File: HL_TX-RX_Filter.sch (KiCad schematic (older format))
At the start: 184 parts, among them J1 To Antenna, J2 From Tx, J3 ICSP, J4 Data In, J5 SCL SDA, J6 To Rx in, Q1 2N7002, Q2 2N7002, Q3 2N7002, Q4 2N7002, Q5 2N7002, Q6 2N7002, Q7 2N7002, Q8 2N7002, U1 LD1117S33TR, U10 PE4259, U11 PE4259, U12 PE4259, U13 PE4259, U2 ATMEGA328-AU, U3 PE4259, U4 PE4259, U5 PE4259, U6 PE4259, U7 PE4259, U8 PE4259, U9 PE4259

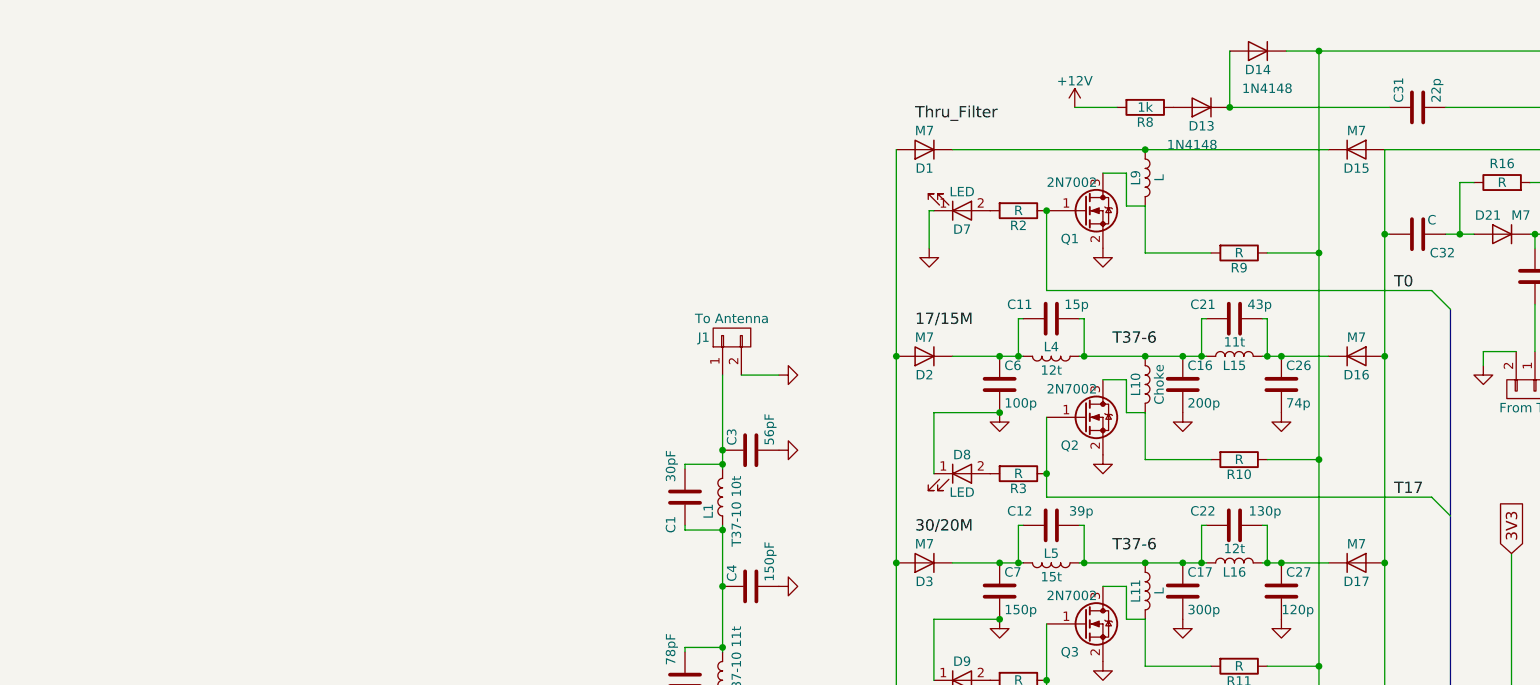
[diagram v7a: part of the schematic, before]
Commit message: More progress with Tx filter board layout
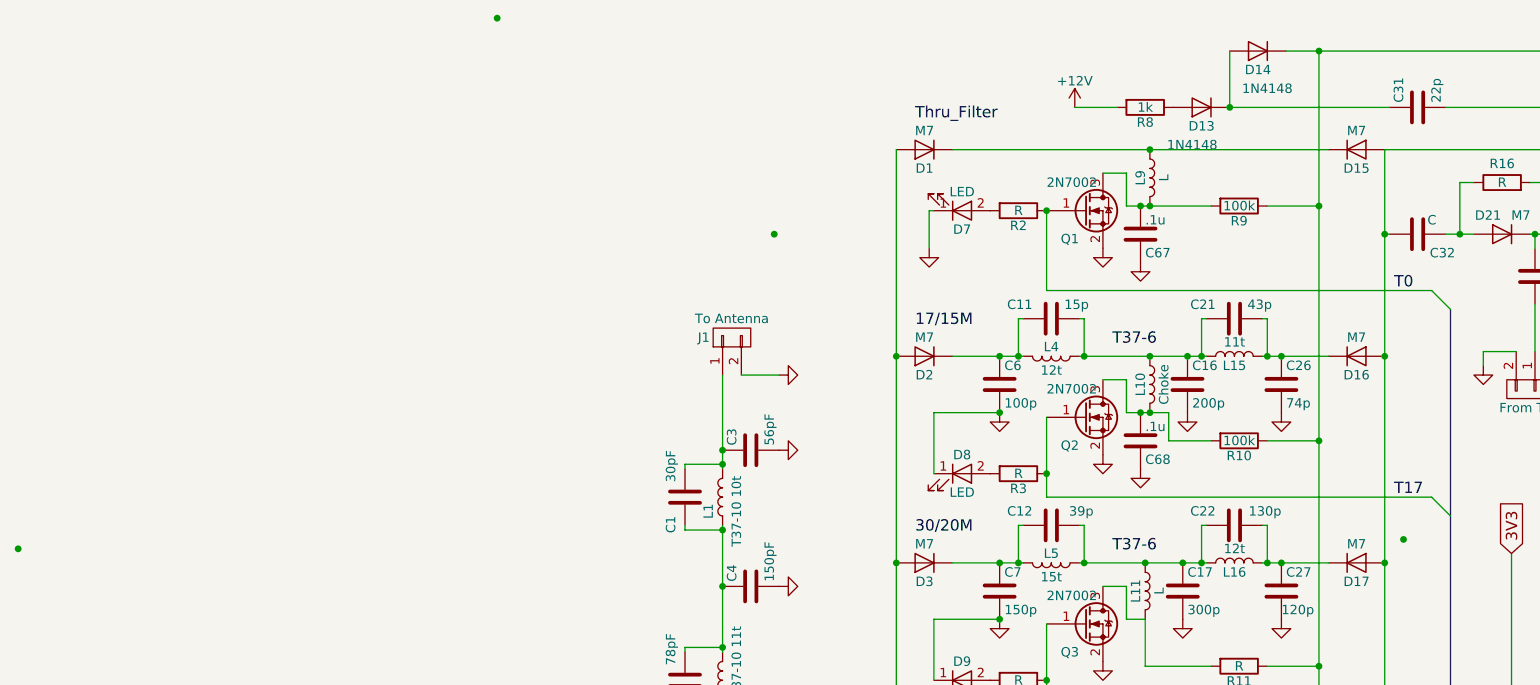
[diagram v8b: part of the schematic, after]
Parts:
- added C67, C68: .1u, Capacitors_SMD:C_1206_HandSoldering, symbol C
- R10, R9: value R -> 100k
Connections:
- net GND: now also C67.2, C68.2
- net at L10.2, Q2.3 (D), R10.2: now also C68.1
- net at L9.2, Q1.3 (D), R9.2: now also C67.1
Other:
- moved on the sheet: C16, L10, L9, R10, R9
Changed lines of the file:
@@
 L C C16
 U 1 1 58EF6AB2
-P 3475 2375
-F 0 "C16" H 3500 2475 50  0000 L CNN
-F 1 "200p" H 3500 2275 50  0000 L CNN
-F 2 "Capacitors_SMD:C_1206_HandSoldering" H 3513 2225 50  0001 C CNN
-F 3 "" H 3475 2375 50  0001 C CNN
-	1    3475 2375
+P 3500 2375
+F 0 "C16" H 3525 2475 50  0000 L CNN
+F 1 "200p" H 3525 2275 50  0000 L CNN
+F 2 "Capacitors_SMD:C_1206_HandSoldering" H 3538 2225 50  0001 C CNN
+F 3 "" H 3500 2375 50  0001 C CNN
+	1    3500 2375
 	1    0    0    -1
 $EndComp
@@
 L GND #PWR027
 U 1 1 58EF6AB8
-P 3475 2525
-F 0 "#PWR027" H 3475 2275 50  0001 C CNN
-F 1 "GND" H 3475 2375 50  0001 C CNN
-F 2 "" H 3475 2525 50  0001 C CNN
-F 3 "" H 3475 2525 50  0001 C CNN
-	1    3475 2525
+P 3500 2525
+F 0 "#PWR027" H 3500 2275 50  0001 C CNN
+F 1 "GND" H 3500 2375 50  0001 C CNN
+F 2 "" H 3500 2525 50  0001 C CNN
+F 3 "" H 3500 2525 50  0001 C CNN
+	1    3500 2525
 	1    0    0    -1
 $EndComp
@@
 L L L10
 U 1 1 58EF6AE3
-P 3275 2375
-F 0 "L10" V 3225 2375 50  0000 C CNN
-F 1 "Choke" V 3350 2375 50  0000 C CNN
-F 2 "Inductors_G:BalunCoreChoke" H 3275 2375 50  0001 C CNN
-F 3 "" H 3275 2375 50  0001 C CNN
-	1    3275 2375
+P 3300 2375
+F 0 "L10" V 3250 2375 50  0000 C CNN
+F 1 "Choke" V 3375 2375 50  0000 C CNN
+F 2 "Inductors_G:BalunCoreChoke" H 3300 2375 50  0001 C CNN
+F 3 "" H 3300 2375 50  0001 C CNN
+	1    3300 2375
 	1    0    0    -1
 $EndComp
@@
 L R R10
 U 1 1 58EF6AFC
-P 3775 2775
-F 0 "R10" V 3855 2775 50  0000 C CNN
-F 1 "R" V 3775 2775 50  0000 C CNN
-F 2 "Resistors_SMD:R_1206_HandSoldering" V 3705 2775 50  0001 C CNN
-F 3 "" H 3775 2775 50  0001 C CNN
-	1    3775 2775
+P 3775 2675
+F 0 "R10" V 3855 2675 50  0000 C CNN
+F 1 "100k" V 3775 2675 50  0000 C CNN
+F 2 "Resistors_SMD:R_1206_HandSoldering" V 3705 2675 50  0001 C CNN
+F 3 "" H 3775 2675 50  0001 C CNN
+	1    3775 2675
 	0    1    1    0
 $EndComp
@@
 L L L9
 U 1 1 58F03CDB
-P 3275 1275
-F 0 "L9" V 3225 1275 50  0000 C CNN
-F 1 "L" V 3350 1275 50  0000 C CNN
-F 2 "Inductors_G:BalunCoreChoke" H 3275 1275 50  0001 C CNN
-F 3 "" H 3275 1275 50  0001 C CNN
-	1    3275 1275
+P 3300 1275
+F 0 "L9" V 3250 1275 50  0000 C CNN
+F 1 "L" V 3375 1275 50  0000 C CNN
+F 2 "Inductors_G:BalunCoreChoke" H 3300 1275 50  0001 C CNN
+F 3 "" H 3300 1275 50  0001 C CNN
+	1    3300 1275
 	1    0    0    -1
 $EndComp
@@
 L R R9
 U 1 1 58F03CF4
-P 3775 1675
-F 0 "R9" V 3855 1675 50  0000 C CNN
-F 1 "R" V 3775 1675 50  0000 C CNN
-F 2 "Resistors_SMD:R_1206_HandSoldering" V 3705 1675 50  0001 C CNN
-F 3 "" H 3775 1675 50  0001 C CNN
-	1    3775 1675
+P 3775 1425
+F 0 "R9" V 3855 1425 50  0000 C CNN
+F 1 "100k" V 3775 1425 50  0000 C CNN
+F 2 "Resistors_SMD:R_1206_HandSoldering" V 3705 1425 50  0001 C CNN
+F 3 "" H 3775 1425 50  0001 C CNN
+	1    3775 1425
 	0    1    1    0
 $EndComp
@@
 Connection ~ 2950 2225
 Connection ~ 2500 2225
-Connection ~ 3475 2225
-Connection ~ 3275 2225
+Connection ~ 3500 2225
+Connection ~ 3300 2225
 Wire Wire Line
 	3050 2350 3175 2350
@@
 	3175 2350 3175 2525
 Wire Wire Line
-	3175 2525 3275 2525
-Wire Wire Line
-	3275 2525 3275 2775
-Wire Wire Line
-	3275 2775 3625 2775
+	3175 2525 3400 2525
+Wire Wire Line
+	3400 2675 3625 2675
 Wire Wire Line
 	1025 4100 1025 4950
@@
 	3175 1250 3175 1425
 Wire Wire Line
-	3175 1425 3275 1425
-Wire Wire Line
-	3275 1425 3275 1675
-Wire Wire Line
-	3275 1675 3625 1675
+	3175 1425 3625 1425
 Wire Wire Line
 	4025 600  7325 600
@@
 Connection ~ 4200 3875
 Wire Wire Line
-	3925 2775 4200 2775
-Connection ~ 4200 2775
-Wire Wire Line
-	3925 1675 4200 1675
-Connection ~ 4200 1675
+	3925 2675 4200 2675
+Connection ~ 4200 2675
+Wire Wire Line
+	3925 1425 4200 1425
+Connection ~ 4200 1425
 Connection ~ 1950 2225
 Connection ~ 1950 3325
@@
 Wire Wire Line
 	2250 1125 4250 1125
-Connection ~ 3275 1125
+Connection ~ 3300 1125
 Wire Wire Line
 	1025 4950 1950 4950
@@
 Connection ~ 8525 3850
 Connection ~ 8525 2800
+$Comp
+L C C68
+U 1 1 596F457D
+P 3250 2675
+F 0 "C68" H 3275 2575 50  0000 L CNN
+F 1 ".1u" H 3275 2750 50  0000 L CNN
+F 2 "Capacitors_SMD:C_1206_HandSoldering" H 3288 2525 50  0001 C CNN
+F 3 "" H 3250 2675 50  0001 C CNN
+	1    3250 2675
+	1    0    0    -1
+$EndComp
+$Comp
+L GND #PWR066
+U 1 1 596F4800
+P 3250 2825
+F 0 "#PWR066" H 3250 2575 50  0001 C CNN
+F 1 "GND" H 3250 2675 50  0001 C CNN
+F 2 "" H 3250 2825 50  0001 C CNN
+F 3 "" H 3250 2825 50  0001 C CNN
+	1    3250 2825
+	1    0    0    -1
+$EndComp
+Wire Wire Line
+	3400 2525 3400 2675
+Connection ~ 3300 2525
+Connection ~ 3250 2525
+$Comp
+L C C67
+U 1 1 596F6C79
+P 3250 1575
+F 0 "C67" H 3275 1475 50  0000 L CNN
+F 1 ".1u" H 3275 1650 50  0000 L CNN
+F 2 "Capacitors_SMD:C_1206_HandSoldering" H 3288 1425 50  0001 C CNN
+F 3 "" H 3250 1575 50  0001 C CNN
+	1    3250 1575
+	1    0    0    -1
+$EndComp
+$Comp
+L GND #PWR067
+U 1 1 596F6C7F
+P 3250 1725
+F 0 "#PWR067" H 3250 1475 50  0001 C CNN
+F 1 "GND" H 3250 1575 50  0001 C CNN
+F 2 "" H 3250 1725 50  0001 C CNN
+F 3 "" H 3250 1725 50  0001 C CNN
+	1    3250 1725
+	1    0    0    -1
+$EndComp
+Connection ~ 3300 1425
+Connection ~ 3250 1425
+Connection ~ 1300 1575
+Connection ~ 4650 3200
+Connection ~ -175 425
+Connection ~ -2725 3250
 $EndSCHEMATC
